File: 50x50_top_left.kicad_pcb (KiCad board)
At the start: 2 copper layers, 48.9 x 48.3 mm, 106 parts, among them CON1 BARREL_JACK, CON2 USB_FEMALE_WITH_ID, CON3 USB_FEMALE_WITH_ID, J1 INTERCONNECT_1X03, J10 INTERCONNECT_1X03, J11 INTERCONNECT_1X03, J12 INTERCONNECT_1X03, J13 INTERCONNECT_1X03, J14 INTERCONNECT_1X03, J15 INTERCONNECT_1X03, J16 INTERCONNECT_1X03, J17 INTERCONNECT_1X03, J18 INTERCONNECT_1X03, J19 INTERCONNECT_1X03, J2 INTERCONNECT_1X03, J20 INTERCONNECT_1X03, J21 INTERCONNECT_1X03, J22 INTERCONNECT_1X03, J23 INTERCONNECT_1X03, J24 INTERCONNECT_1X03, J25 INTERCONNECT_1X03, J26 INTERCONNECT_1X03, J27 INTERCONNECT_1X03, J28 INTERCONNECT_1X03, J29 INTERCONNECT_1X03, J3 INTERCONNECT_1X03, J30 INTERCONNECT_1X03, J31 INTERCONNECT_1X03, J32 INTERCONNECT_1X03, J33 INTERCONNECT_1X03, J34 INTERCONNECT_1X03, J35 INTERCONNECT_1X03, J36 INTERCONNECT_1X03, J37 INTERCONNECT_1X03, J38 INTERCONNECT_1X03, J39 INTERCONNECT_1X03, J4 INTERCONNECT_1X03, J40 INTERCONNECT_1X03, J41 INTERCONNECT_1X03, J42 INTERCONNECT_1X03, J43 INTERCONNECT_1X03, J44 INTERCONNECT_1X03, J45 INTERCONNECT_1X03, J46 INTERCONNECT_1X03, J47 INTERCONNECT_1X03, J48 INTERCONNECT_1X03, J49 INTERCONNECT_1X03, J5 INTERCONNECT_1X03, J50 INTERCONNECT_1X03, J51 INTERCONNECT_1X03, J52 INTERCONNECT_1X03, J53 INTERCONNECT_1X03, J54 INTERCONNECT_1X03, J55 INTERCONNECT_1X03, J56 INTERCONNECT_1X03, J57 INTERCONNECT_1X03, J58 INTERCONNECT_1X03, J59 INTERCONNECT_1X03, J6 INTERCONNECT_1X03, J60 INTERCONNECT_1X03, J61 INTERCONNECT_1X03, J62 INTERCONNECT_1X03, J63 INTERCONNECT_1X03, J64 INTERCONNECT_1X03, J65 INTERCONNECT_1X02, J7 INTERCONNECT_1X03, J8 INTERCONNECT_1X03, J9 INTERCONNECT_1X03, P1 CONN_5, U1 LM7805CT

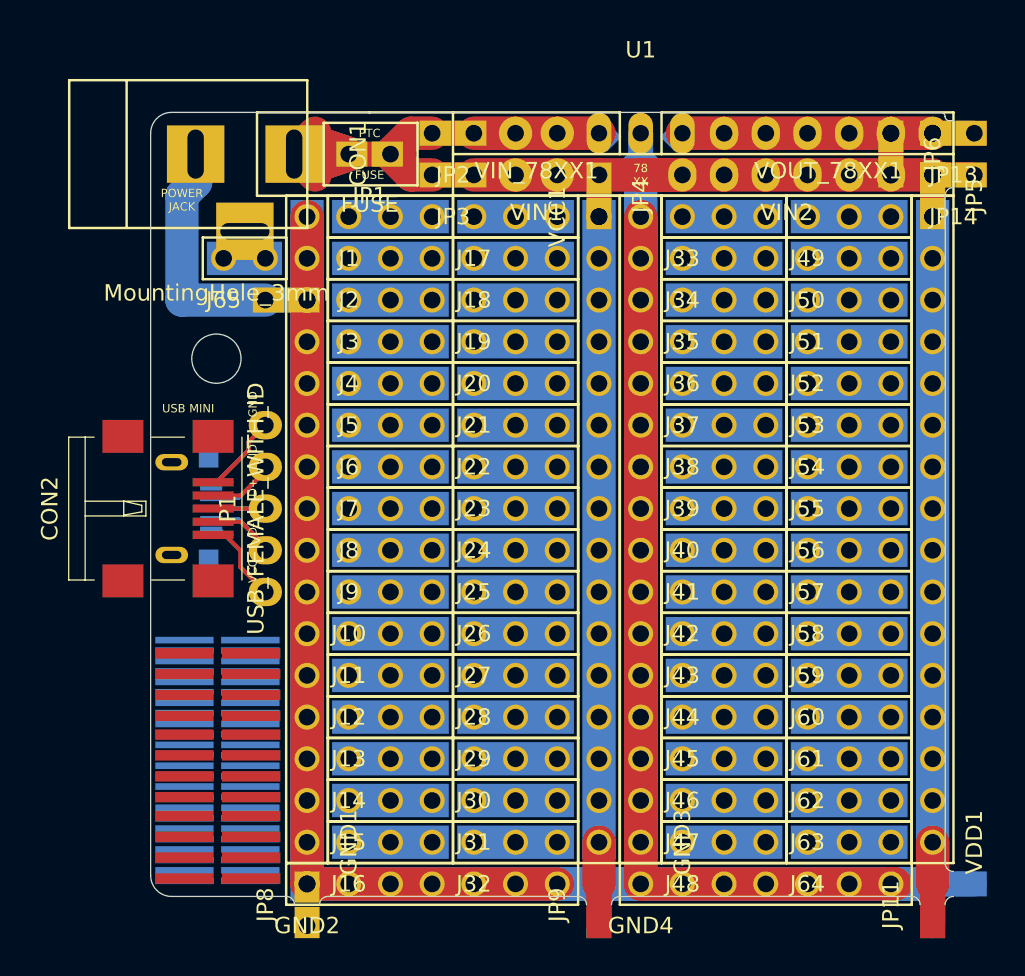
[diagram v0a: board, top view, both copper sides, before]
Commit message: added 3*3 mouse bites between the sub-boards on both edges
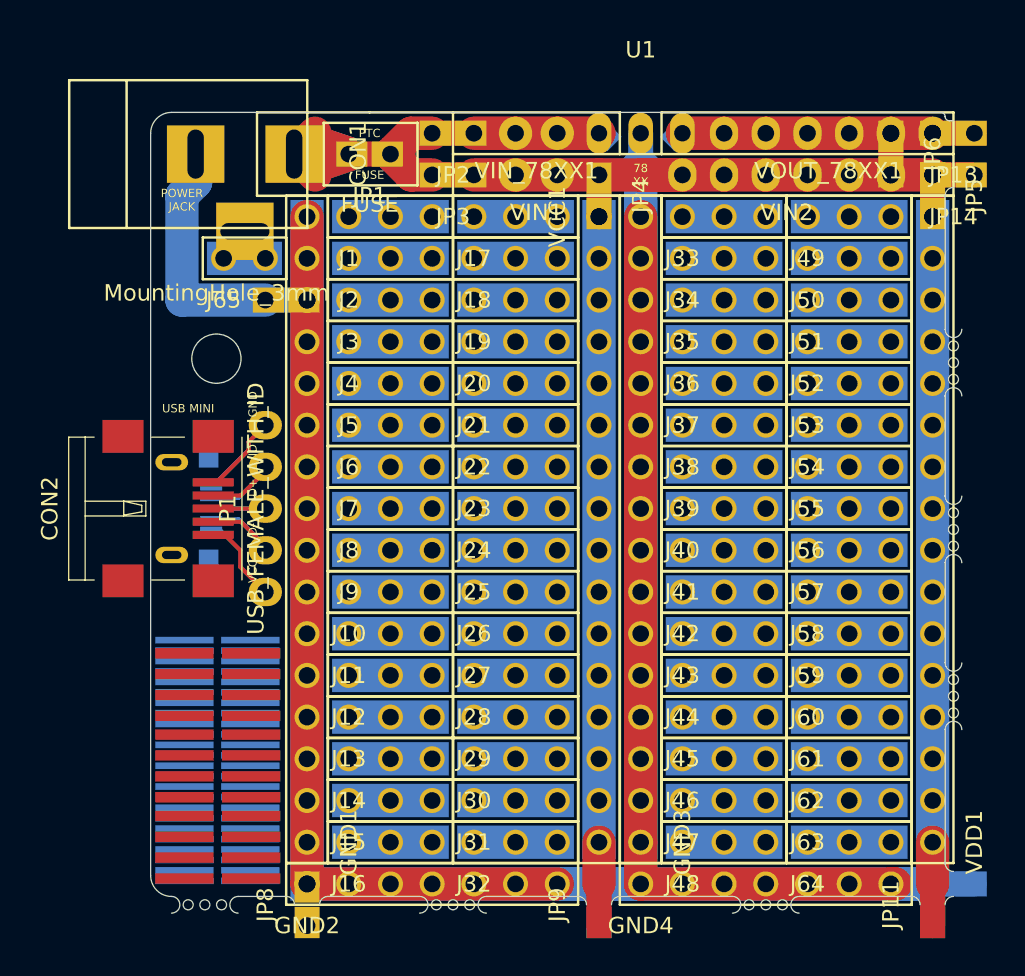
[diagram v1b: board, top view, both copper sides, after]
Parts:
- added Mouse_Bites_3_1.27mm: VAL**, Misc:Mouse_Bites_3_1.016mm, F.Cu at (78.7, 39.1)
- added Mouse_Bites_3_1.27mm: VAL**, Misc:Mouse_Bites_3_1.016mm, F.Cu at (78.7, 49.3)
- added Mouse_Bites_3_1.27mm: VAL**, Misc:Mouse_Bites_3_1.016mm, F.Cu at (78.7, 59.4)
- added Mouse_Bites_3_1.27mm: VAL**, Misc:Mouse_Bites_3_1.016mm, F.Cu at (66.3, 71.1)
- added Mouse_Bites_3_1.27mm: VAL**, Misc:Mouse_Bites_3_1.016mm, F.Cu at (47.2, 71.1)
- added Mouse_Bites_3_1.27mm: VAL**, Misc:Mouse_Bites_3_1.016mm, F.Cu at (32.1, 71.1)
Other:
- outline, holes or cut-outs redrawn
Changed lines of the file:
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@@
     (links 341)
     (no_connects 10)
-    (area 18.365667 17.871 83.267572 73.5965)
+    (area 18.365667 17.871 86.054715 73.699)
     (thickness 1.6)
-    (drawings 66)
+    (drawings 71)
     (tracks 88)
     (zones 0)
-    (modules 106)
+    (modules 112)
     (nets 90)
   )
@@
       (net 2 "Net-(C1-Pad2)"))
   )
+  (module Misc:Mouse_Bites_3_1.016mm (layer F.Cu)
+    (at 78.74 39.116 90)
+    (fp_text reference Mouse_Bites_3_1.27mm (at 0 -1.8 90) (layer F.SilkS) hide
+      (effects (font (size 1 1) (thickness 0.15)))
+    )
+    (fp_text value VAL** (at 0 1.55 90) (layer F.SilkS) hide
+      (effects (font (size 1 1) (thickness 0.15)))
+    )
+    (fp_arc (start -1.016 0) (end -1.016 -0.508) (angle 180) (layer Edge.Cuts) (width 0.0254))
+    (fp_arc (start 3.048 0) (end 3.048 0.508) (angle 180) (layer Edge.Cuts) (width 0.0254))
+    (pad "" np_thru_hole circle (at 2.032 0 90) (size 0.6096 0.6096) (drill 0.6096) (layers *.Cu *.Mask F.SilkS)
+      (clearance 0.2032))
+    (pad "" np_thru_hole circle (at 1.016 0 90) (size 0.6096 0.6096) (drill 0.6096) (layers *.Cu *.Mask F.SilkS)
+      (clearance 0.2032))
+    (pad "" np_thru_hole circle (at 0 0 90) (size 0.6096 0.6096) (drill 0.6096) (layers *.Cu *.Mask F.SilkS)
+      (clearance 0.2032))
+  )
+  (module Misc:Mouse_Bites_3_1.016mm (layer F.Cu)
+    (at 78.74 49.276 90)
+    (fp_text reference Mouse_Bites_3_1.27mm (at 0 -1.8 90) (layer F.SilkS) hide
+      (effects (font (size 1 1) (thickness 0.15)))
+    )
+    (fp_text value VAL** (at 0 1.55 90) (layer F.SilkS) hide
+      (effects (font (size 1 1) (thickness 0.15)))
+    )
+    (fp_arc (start -1.016 0) (end -1.016 -0.508) (angle 180) (layer Edge.Cuts) (width 0.0254))
+    (fp_arc (start 3.048 0) (end 3.048 0.508) (angle 180) (layer Edge.Cuts) (width 0.0254))
+    (pad "" np_thru_hole circle (at 2.032 0 90) (size 0.6096 0.6096) (drill 0.6096) (layers *.Cu *.Mask F.SilkS)
+      (clearance 0.2032))
+    (pad "" np_thru_hole circle (at 1.016 0 90) (size 0.6096 0.6096) (drill 0.6096) (layers *.Cu *.Mask F.SilkS)
+      (clearance 0.2032))
+    (pad "" np_thru_hole circle (at 0 0 90) (size 0.6096 0.6096) (drill 0.6096) (layers *.Cu *.Mask F.SilkS)
+      (clearance 0.2032))
+  )
+  (module Misc:Mouse_Bites_3_1.016mm (layer F.Cu)
+    (at 78.74 59.436 90)
+    (fp_text reference Mouse_Bites_3_1.27mm (at 0 -1.8 90) (layer F.SilkS) hide
+      (effects (font (size 1 1) (thickness 0.15)))
+    )
+    (fp_text value VAL** (at 0 1.55 90) (layer F.SilkS) hide
+      (effects (font (size 1 1) (thickness 0.15)))
+    )
+    (fp_arc (start -1.016 0) (end -1.016 -0.508) (angle 180) (layer Edge.Cuts) (width 0.0254))
+    (fp_arc (start 3.048 0) (end 3.048 0.508) (angle 180) (layer Edge.Cuts) (width 0.0254))
+    (pad "" np_thru_hole circle (at 2.032 0 90) (size 0.6096 0.6096) (drill 0.6096) (layers *.Cu *.Mask F.SilkS)
+      (clearance 0.2032))
+    (pad "" np_thru_hole circle (at 1.016 0 90) (size 0.6096 0.6096) (drill 0.6096) (layers *.Cu *.Mask F.SilkS)
+      (clearance 0.2032))
+    (pad "" np_thru_hole circle (at 0 0 90) (size 0.6096 0.6096) (drill 0.6096) (layers *.Cu *.Mask F.SilkS)
+      (clearance 0.2032))
+  )
+  (module Misc:Mouse_Bites_3_1.016mm (layer F.Cu)
+    (at 66.294 71.12)
+    (fp_text reference Mouse_Bites_3_1.27mm (at 0 -1.8) (layer F.SilkS) hide
+      (effects (font (size 1 1) (thickness 0.15)))
+    )
+    (fp_text value VAL** (at 0 1.55) (layer F.SilkS) hide
+      (effects (font (size 1 1) (thickness 0.15)))
+    )
+    (fp_arc (start -1.016 0) (end -1.016 -0.508) (angle 180) (layer Edge.Cuts) (width 0.0254))
+    (fp_arc (start 3.048 0) (end 3.048 0.508) (angle 180) (layer Edge.Cuts) (width 0.0254))
+    (pad "" np_thru_hole circle (at 2.032 0) (size 0.6096 0.6096) (drill 0.6096) (layers *.Cu *.Mask F.SilkS)
+      (clearance 0.2032))
+    (pad "" np_thru_hole circle (at 1.016 0) (size 0.6096 0.6096) (drill 0.6096) (layers *.Cu *.Mask F.SilkS)
+      (clearance 0.2032))
+    (pad "" np_thru_hole circle (at 0 0) (size 0.6096 0.6096) (drill 0.6096) (layers *.Cu *.Mask F.SilkS)
+      (clearance 0.2032))
+  )
+  (module Misc:Mouse_Bites_3_1.016mm (layer F.Cu)
+    (at 47.244 71.12)
+    (fp_text reference Mouse_Bites_3_1.27mm (at 0 -1.8) (layer F.SilkS) hide
+      (effects (font (size 1 1) (thickness 0.15)))
+    )
+    (fp_text value VAL** (at 0 1.55) (layer F.SilkS) hide
+      (effects (font (size 1 1) (thickness 0.15)))
+    )
+    (fp_arc (start -1.016 0) (end -1.016 -0.508) (angle 180) (layer Edge.Cuts) (width 0.0254))
+    (fp_arc (start 3.048 0) (end 3.048 0.508) (angle 180) (layer Edge.Cuts) (width 0.0254))
+    (pad "" np_thru_hole circle (at 2.032 0) (size 0.6096 0.6096) (drill 0.6096) (layers *.Cu *.Mask F.SilkS)
+      (clearance 0.2032))
+    (pad "" np_thru_hole circle (at 1.016 0) (size 0.6096 0.6096) (drill 0.6096) (layers *.Cu *.Mask F.SilkS)
+      (clearance 0.2032))
+    (pad "" np_thru_hole circle (at 0 0) (size 0.6096 0.6096) (drill 0.6096) (layers *.Cu *.Mask F.SilkS)
+      (clearance 0.2032))
+  )
+  (module Misc:Mouse_Bites_3_1.016mm (layer F.Cu)
+    (at 32.131 71.12)
+    (fp_text reference Mouse_Bites_3_1.27mm (at 0 -1.8) (layer F.SilkS) hide
+      (effects (font (size 1 1) (thickness 0.15)))
+    )
+    (fp_text value VAL** (at 0 1.55) (layer F.SilkS) hide
+      (effects (font (size 1 1) (thickness 0.15)))
+    )
+    (fp_arc (start -1.016 0) (end -1.016 -0.508) (angle 180) (layer Edge.Cuts) (width 0.0254))
+    (fp_arc (start 3.048 0) (end 3.048 0.508) (angle 180) (layer Edge.Cuts) (width 0.0254))
+    (pad "" np_thru_hole circle (at 2.032 0) (size 0.6096 0.6096) (drill 0.6096) (layers *.Cu *.Mask F.SilkS)
+      (clearance 0.2032))
+    (pad "" np_thru_hole circle (at 1.016 0) (size 0.6096 0.6096) (drill 0.6096) (layers *.Cu *.Mask F.SilkS)
+      (clearance 0.2032))
+    (pad "" np_thru_hole circle (at 0 0) (size 0.6096 0.6096) (drill 0.6096) (layers *.Cu *.Mask F.SilkS)
+      (clearance 0.2032))
+  )
+  (gr_line (start 38.1 70.612) (end 35.179 70.612) (angle 90) (layer Edge.Cuts) (width 0.0254))
+  (gr_line (start 46.228 70.612) (end 40.64 70.612) (angle 90) (layer Edge.Cuts) (width 0.0254))
+  (gr_line (start 55.88 70.612) (end 50.292 70.612) (angle 90) (layer Edge.Cuts) (width 0.0254))
+  (gr_line (start 65.278 70.612) (end 58.42 70.612) (angle 90) (layer Edge.Cuts) (width 0.0254))
+  (gr_line (start 76.2 70.612) (end 69.342 70.612) (angle 90) (layer Edge.Cuts) (width 0.0254))
+  (gr_line (start 78.232 60.452) (end 78.232 68.58) (angle 90) (layer Edge.Cuts) (width 0.0254))
+  (gr_line (start 78.232 50.292) (end 78.232 56.388) (angle 90) (layer Edge.Cuts) (width 0.0254))
+  (gr_line (start 78.232 40.132) (end 78.232 46.228) (angle 90) (layer Edge.Cuts) (width 0.0254))
+  (gr_line (start 78.232 27.94) (end 78.232 36.068) (angle 90) (layer Edge.Cuts) (width 0.0254))
   (gr_text 100n (at 60.4774 27.051 45) (layer B.SilkS)
     (effects (font (size 0.508 0.508) (thickness 0.127)) (justify mirror))
@@
   (gr_arc (start 78.486 23.114) (end 78.486 23.368) (angle 90) (layer Edge.Cuts) (width 0.0254))
   (gr_line (start 29.845 69.342) (end 29.845 24.13) (angle 90) (layer Edge.Cuts) (width 0.0254))
-  (gr_line (start 31.115 70.612) (end 38.1 70.612) (angle 90) (layer Edge.Cuts) (width 0.0254))
   (gr_arc (start 31.115 69.342) (end 31.115 70.612) (angle 90) (layer Edge.Cuts) (width 0.0254))
   (gr_line (start 36.322 27.94) (end 78.74 27.94) (angle 90) (layer F.SilkS) (width 0.15))
   (gr_arc (start 38.1 71.12) (end 38.1 70.612) (angle 90) (layer Edge.Cuts) (width 0.0254))
   (gr_arc (start 40.64 71.12) (end 40.132 71.12) (angle 90) (layer Edge.Cuts) (width 0.0254))
-  (gr_line (start 55.88 70.612) (end 40.64 70.612) (angle 90) (layer Edge.Cuts) (width 0.0254))
   (gr_arc (start 55.88 71.12) (end 55.88 70.612) (angle 90) (layer Edge.Cuts) (width 0.0254))
   (gr_arc (start 58.42 71.12) (end 57.912 71.12) (angle 90) (layer Edge.Cuts) (width 0.0254))
-  (gr_line (start 76.2 70.612) (end 58.42 70.612) (angle 90) (layer Edge.Cuts) (width 0.0254))
   (gr_arc (start 76.2 71.12) (end 76.2 70.612) (angle 90) (layer Edge.Cuts) (width 0.0254))
   (gr_arc (start 78.74 71.12) (end 78.232 71.12) (angle 90) (layer Edge.Cuts) (width 0.0254))
   (gr_arc (start 78.74 68.58) (end 78.74 69.088) (angle 90) (layer Edge.Cuts) (width 0.0254))
-  (gr_line (start 78.232 27.94) (end 78.232 68.58) (angle 90) (layer Edge.Cuts) (width 0.0254))
   (gr_arc (start 78.74 27.94) (end 78.232 27.94) (angle 90) (layer Edge.Cuts) (width 0.0254))
   (gr_arc (start 31.115 24.13) (end 29.845 24.13) (angle 90) (layer Edge.Cuts) (width 0.0254))
